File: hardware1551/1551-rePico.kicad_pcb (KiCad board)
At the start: 2 copper layers, 62.1 x 101 mm, 37 parts, among them J1 0.96_I2C_OLED, J10 TCBM, J11 JTAG, J6 Rotary encoder, J8 SD CARD, Q1 BSS138, Q2 BSS138, Q3 BSS138, Q4 BSS138, U1 Pico, U3 XC9572XL-VQ64, U4 6523 (pins), U5 6510T (pins), U6 6510T (socket for chip)

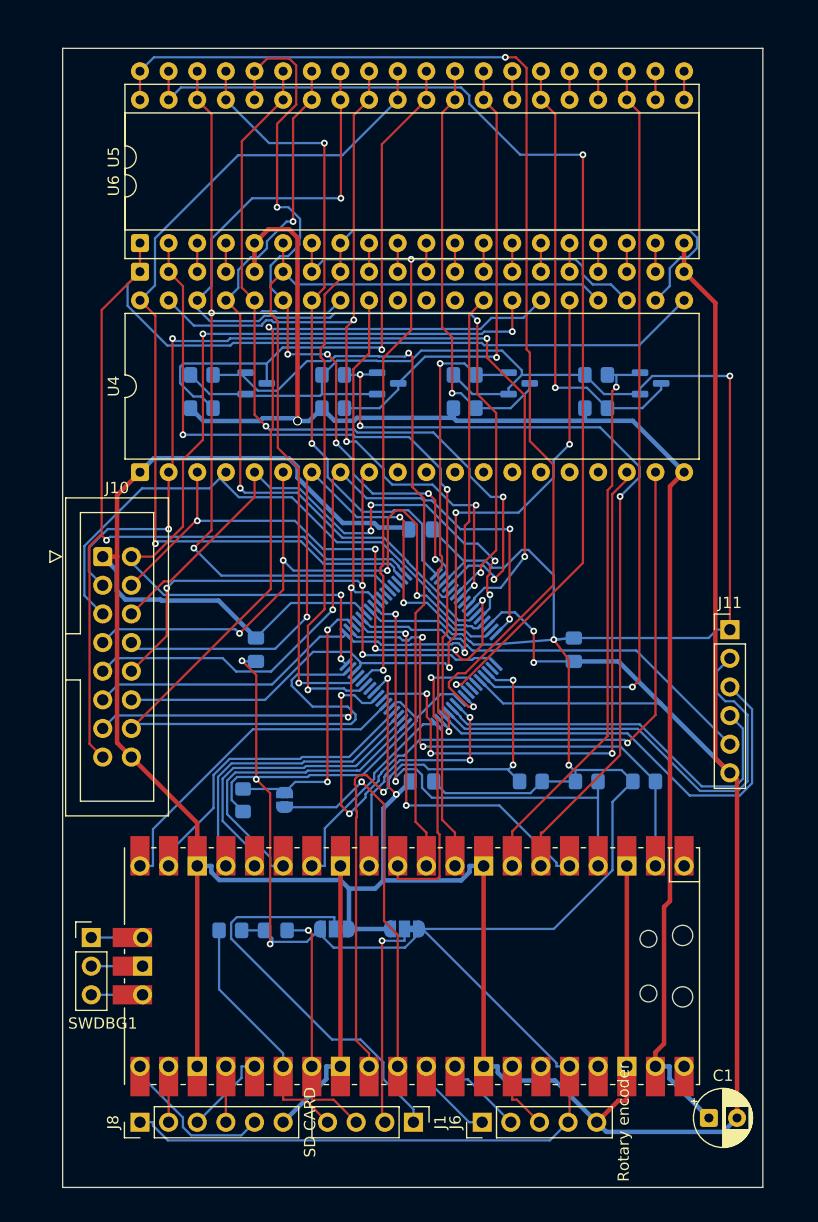
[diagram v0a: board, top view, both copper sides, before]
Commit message: board for 1551 with correct dimensions and spacing between CPU and TPI, routed
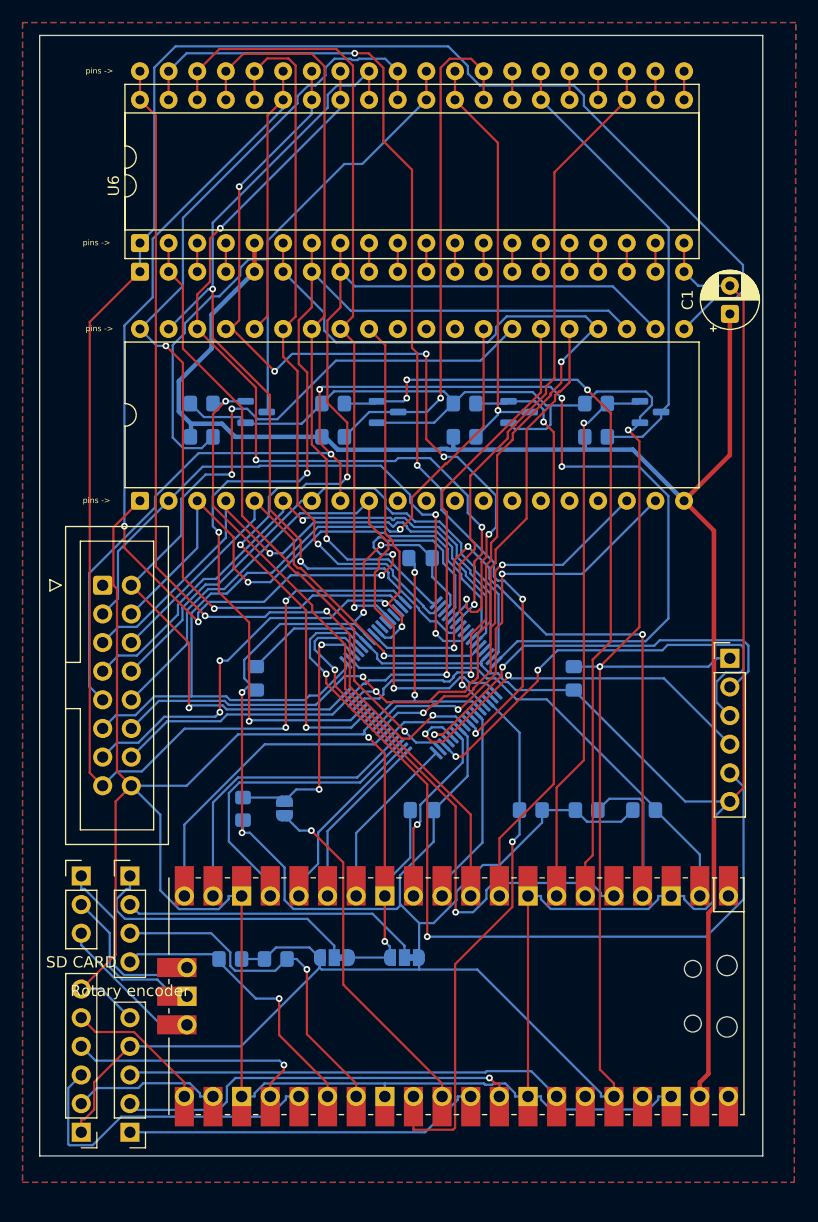
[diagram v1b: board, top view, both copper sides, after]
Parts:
- moved C1 71.3 mm to (159.4, 87.5), turned to 90 degrees
- moved J1 33.3 mm to (106.1, 137.4), turned to 0 degrees
- moved J6 31.3 mm to (106.1, 160.1), turned to 180 degrees
- moved SWDBG1 5.53 mm to (101.8, 137.4)
- moved J8 5.28 mm to (101.8, 160.1), turned to 180 degrees
- moved U1 4.76 mm to (135.1, 148.1)
- moved C4 2.54 mm to (132.0, 131.5)
- moved R11 2.54 mm to (151.8, 131.5)
- moved R12 2.54 mm to (146.7, 131.5)
- moved R13 2.54 mm to (119.1, 144.8)
- moved R14 2.54 mm to (115.0, 144.8)
- moved R8 2.54 mm to (141.7, 131.5)
- moved C2 2.54 mm to (117.3, 119.9)
- moved C3 2.54 mm to (145.5, 119.9)
- moved J10 2.54 mm to (103.7, 111.6)
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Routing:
- net /DIO7: track 63.1 -> 115.2 mm, vias 3 -> 4
- net /~{RESET}: track 132.9 -> 178.5 mm, vias 1 -> 2
- net /D3: track 71.0 -> 115.1 mm, vias 3 -> 4
- net /TDO: track 37.3 -> 77.2 mm, vias 0 -> 2
- net /STATUS1: track 99.7 -> 65.5 mm
- net /ROT_SW: track 6.19 -> 38.9 mm
- net /DIO1: track 84.6 -> 53.5 mm, vias 4 -> 2
- net /XR/~{W}: track 67.6 -> 38.0 mm, vias 3 -> 2
- net GND: track 392.0 -> 363.1 mm
- net /ROT_DT: track 7.68 -> 36.3 mm, vias 0 -> 1
- net /SYNC_3V3: track 45.0 -> 72.5 mm, vias 2 -> 3
- net /ROT_CLK: track 7.68 -> 31.7 mm
- net /SD_MOSI: track 7.73 -> 29.1 mm
- net /PHI2: track 102.0 -> 82.5 mm, vias 2 -> 3
- net /A1: track 72.8 -> 92.2 mm, vias 2 -> 3
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- added copper zone on B.Cu, net GND
- added copper zone on F.Cu, net GND
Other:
- board size 62.1 x 101 mm -> 64.1 x 99.4 mm
- board text added: "pins ->"

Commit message: updates/fixes and review what to do after
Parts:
- J6: value Rotary encoder -> Conn_01x05
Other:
- board text added: "1551-rePico v1.0, VII 2026 by Maciej Witkowiak <ytm@elysium.pl>"
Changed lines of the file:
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@@
 	(paper "A4")
 	(title_block
-		(title "1541-rePico")
-		(date "2026-04-13")
-		(rev "1.6")
+		(title "1551-rePico")
+		(date "2026-07-03")
+		(rev "1.0")
+		(company "YTM Enterprises")
+		(comment 1 "based on 1541-rePico and Fake6523")
 	)
 	(layers
@@
 		(sheetname "/")
 		(sheetfile "1551-rePico.kicad_sch")
-		(attr through_hole)
+		(attr through_hole exclude_from_bom)
 		(fp_line
 			(start 14.08 -1.33)
@@
 			(at 0 15.08 0)
 			(layer "F.SilkS")
+			(hide yes)
 			(effects
 				(font
@@
 		(sheetname "/")
 		(sheetfile "1551-rePico.kicad_sch")
-		(attr through_hole)
+		(attr through_hole exclude_from_bom)
 		(fp_line
 			(start 1.38 1.27)
@@
 		(sheetname "/")
 		(sheetfile "1551-rePico.kicad_sch")
-		(attr through_hole)
+		(attr through_hole exclude_from_bom)
 		(fp_line
 			(start 14.08 -1.33)
@@
 			)
 		)
-		(property "Value" "Rotary encoder"
+		(property "Value" "Conn_01x05"
 			(at 0 12.54 0)
 			(layer "F.SilkS")
+			(hide yes)
 			(effects
 				(font
@@
 			(at 0 10 0)
 			(layer "F.Fab")
+			(hide yes)
 			(effects
 				(font
@@
 		(sheetname "/")
 		(sheetfile "1551-rePico.kicad_sch")
-		(attr through_hole)
+		(attr through_hole exclude_from_bom)
 		(fp_line
 			(start -1.38 -1.38)
@@
 		(sheetname "/")
 		(sheetfile "1551-rePico.kicad_sch")
-		(attr through_hole)
+		(attr through_hole exclude_from_bom)
 		(fp_line
 			(start 14.08 -1.33)
@@
 		(sheetname "/")
 		(sheetfile "1551-rePico.kicad_sch")
-		(attr through_hole)
+		(attr through_hole exclude_from_bom)
 		(fp_line
 			(start 1.29 -2.58)
@@
 		(sheetname "/")
 		(sheetfile "1551-rePico.kicad_sch")
-		(attr through_hole)
+		(attr through_hole exclude_from_bom)
 		(fp_line
 			(start -1.38 -1.38)
@@
 		(sheetname "/")
 		(sheetfile "1551-rePico.kicad_sch")
-		(attr through_hole)
+		(attr through_hole exclude_from_bom)
 		(fp_line
 			(start -3.7 25.5)
@@
 		(sheetname "/")
 		(sheetfile "1551-rePico.kicad_sch")
-		(attr through_hole)
+		(attr through_hole exclude_from_bom)
 		(fp_line
 			(start -1.38 -1.38)
@@
 			)
 		)
+		(property "JLCPCB Part #" "C78284"
+			(at 0 0 0)
+			(unlocked yes)
+			(layer "B.Fab")
+			(hide yes)
+			(effects
+				(font
+					(size 1 1)
+					(thickness 0.15)
+				)
+				(justify mirror)
+			)
+		)
+		(property "JLCPCB URL" "https://jlcpcb.com/partdetail/79418-BSS138/C78284"
+			(at 0 0 0)
+			(unlocked yes)
+			(layer "B.Fab")
+			(hide yes)
+			(effects
+				(font
+					(size 1 1)
+					(thickness 0.15)
+				)
+				(justify mirror)
+			)
+		)
+		(property "MFR.Part #" "BSS138"
+			(at 0 0 0)
+			(unlocked yes)
+			(layer "B.Fab")
+			(hide yes)
+			(effects
+				(font
+					(size 1 1)
+					(thickness 0.15)
+				)
+				(justify mirror)
+			)
+		)
 		(property ki_fp_filters "SOT?23*")
 		(sheetname "/BSS138_7/")
@@
 			)
 		)
+		(property "JLCPCB Part #" "C78284"
+			(at 0 0 0)
+			(unlocked yes)
+			(layer "B.Fab")
+			(hide yes)
+			(effects
+				(font
+					(size 1 1)
+					(thickness 0.15)
+				)
+				(justify mirror)
+			)
+		)
+		(property "JLCPCB URL" "https://jlcpcb.com/partdetail/79418-BSS138/C78284"
+			(at 0 0 0)
+			(unlocked yes)
+			(layer "B.Fab")
+			(hide yes)
+			(effects
+				(font
+					(size 1 1)
+					(thickness 0.15)
+				)
+				(justify mirror)
+			)
+		)
+		(property "MFR.Part #" "BSS138"
+			(at 0 0 0)
+			(unlocked yes)
+			(layer "B.Fab")
+			(hide yes)
+			(effects
+				(font
+					(size 1 1)
+					(thickness 0.15)
+				)
+				(justify mirror)
+			)
+		)
 		(property ki_fp_filters "SOT?23*")
 		(sheetname "/BSS138_9/")
@@
 			)
 		)
+		(property "JLCPCB Part #" "C78284"
+			(at 0 0 0)
+			(unlocked yes)
+			(layer "B.Fab")
+			(hide yes)
+			(effects
+				(font
+					(size 1 1)
+					(thickness 0.15)
+				)
+				(justify mirror)
+			)
+		)
+		(property "JLCPCB URL" "https://jlcpcb.com/partdetail/79418-BSS138/C78284"
+			(at 0 0 0)
+			(unlocked yes)
+			(layer "B.Fab")
+			(hide yes)
+			(effects
+				(font
+					(size 1 1)
+					(thickness 0.15)
+				)
+				(justify mirror)
+			)
+		)
+		(property "MFR.Part #" "BSS138"
+			(at 0 0 0)
+			(unlocked yes)
+			(layer "B.Fab")
+			(hide yes)
+			(effects
+				(font
+					(size 1 1)
+					(thickness 0.15)
+				)
+				(justify mirror)
+			)
+		)
 		(property ki_fp_filters "SOT?23*")
 		(sheetname "/BSS138_6/")
@@
 			)
 		)
+		(property "JLCPCB Part #" "C78284"
+			(at 0 0 0)
+			(unlocked yes)
+			(layer "B.Fab")
+			(hide yes)
+			(effects
+				(font
+					(size 1 1)
+					(thickness 0.15)
+				)
+				(justify mirror)
+			)
+		)
+		(property "JLCPCB URL" "https://jlcpcb.com/partdetail/79418-BSS138/C78284"
+			(at 0 0 0)
+			(unlocked yes)
+			(layer "B.Fab")
+			(hide yes)
+			(effects
+				(font
+					(size 1 1)
+					(thickness 0.15)
+				)
+				(justify mirror)
+			)
+		)
+		(property "MFR.Part #" "BSS138"
+			(at 0 0 0)
+			(unlocked yes)
+			(layer "B.Fab")
+			(hide yes)
+			(effects
+				(font
+					(size 1 1)
+					(thickness 0.15)
+				)
+				(justify mirror)
+			)
+		)
 		(property ki_fp_filters "SOT?23*")
 		(sheetname "/BSS138_8/")
@@
 		)
 	)
+	(gr_text "1551-rePico v1.0, VII 2026\nby Maciej Witkowiak <ytm@elysium.pl>"
+		(at 131.9276 109.8296 0)
+		(layer "F.SilkS")
+		(effects
+			(font
+				(size 1 1)
+				(thickness 0.1)
+			)
+			(justify bottom)
+		)
+	)
